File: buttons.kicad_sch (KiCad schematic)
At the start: 16 parts

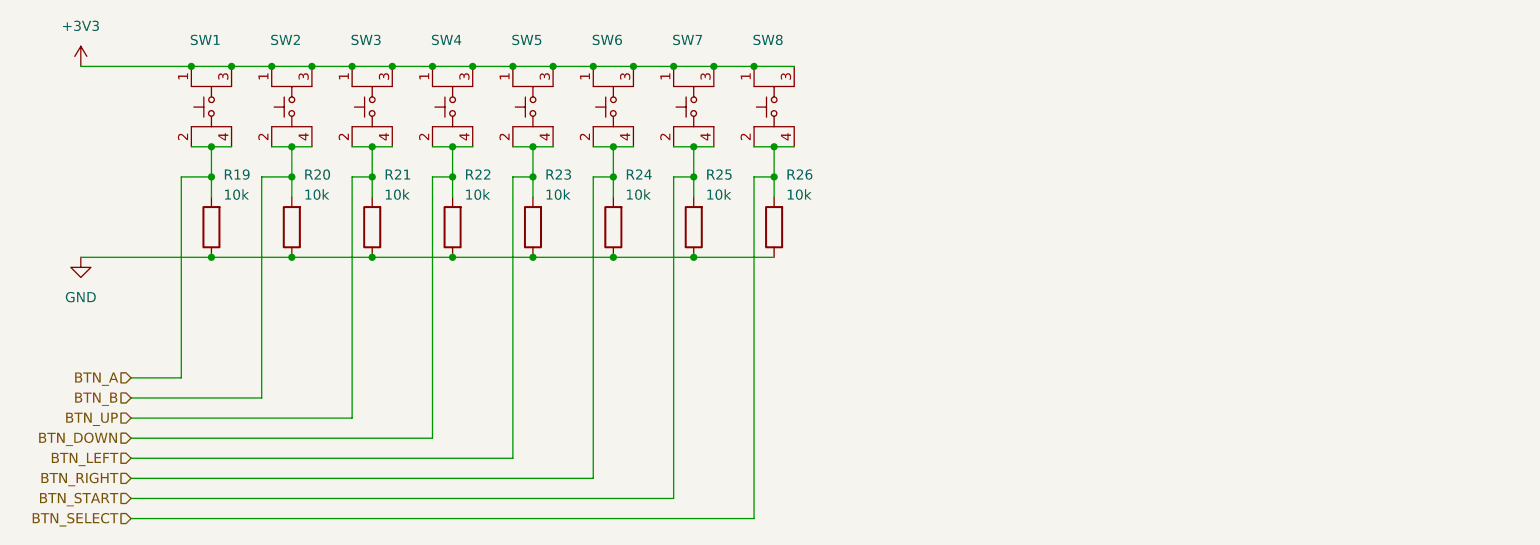
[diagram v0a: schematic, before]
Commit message: button debouncing and VDD decoupling
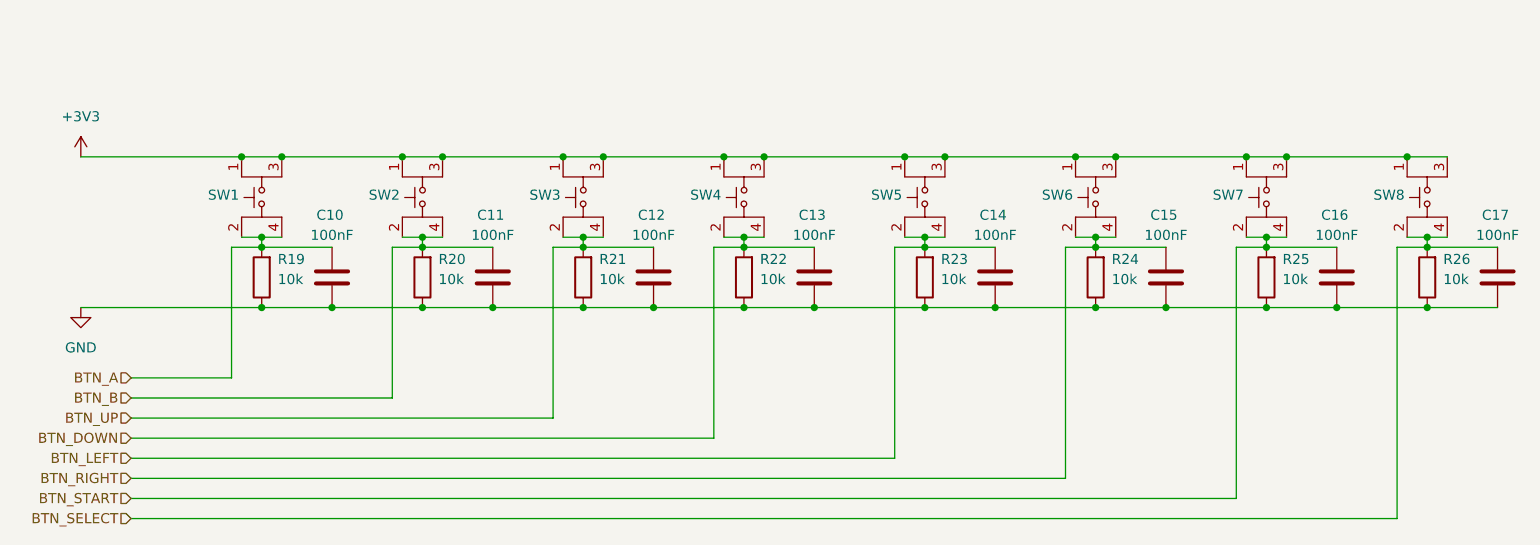
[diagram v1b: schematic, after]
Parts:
- added C10, C11, C12, C13, C14, C15, C16, C17: 100nF, Capacitor_SMD:C_0603_1608Metric, symbol Device:C
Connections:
- net BTN_A: now also C10.2
- net BTN_B: now also C11.2
- net BTN_DOWN: now also C13.2
- net BTN_LEFT: now also C14.2
- net BTN_RIGHT: now also C15.2
- net BTN_SELECT: now also C17.2
- net BTN_START: now also C16.2
- net BTN_UP: now also C12.2
- net GND: now also C10.1, C11.1, C12.1, C13.1, C14.1, C15.1, C16.1, C17.1
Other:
- moved on the sheet: R19, SW1

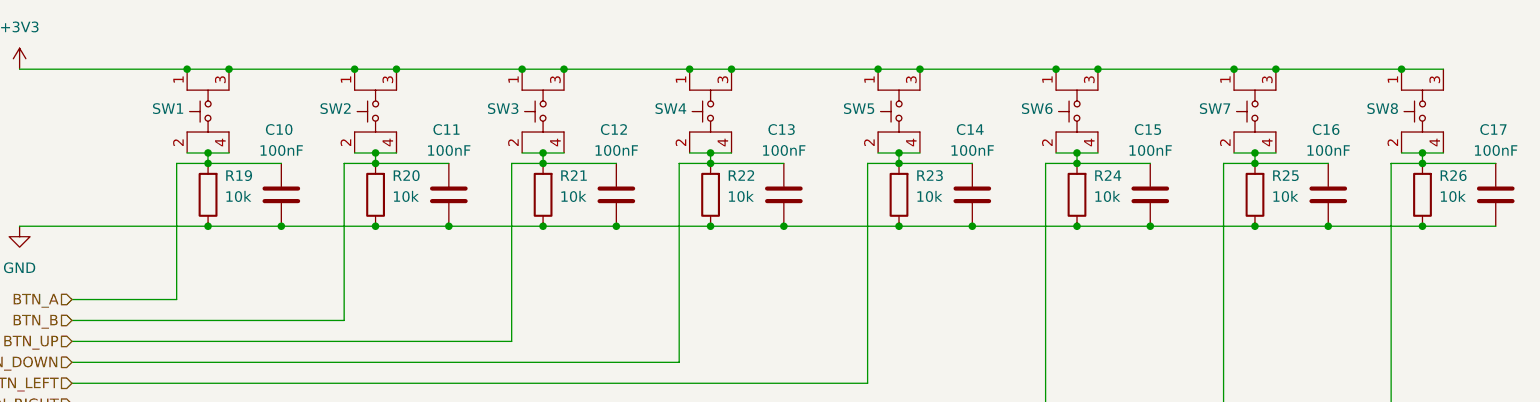
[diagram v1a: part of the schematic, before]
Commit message: schematic functional and includes current test setup
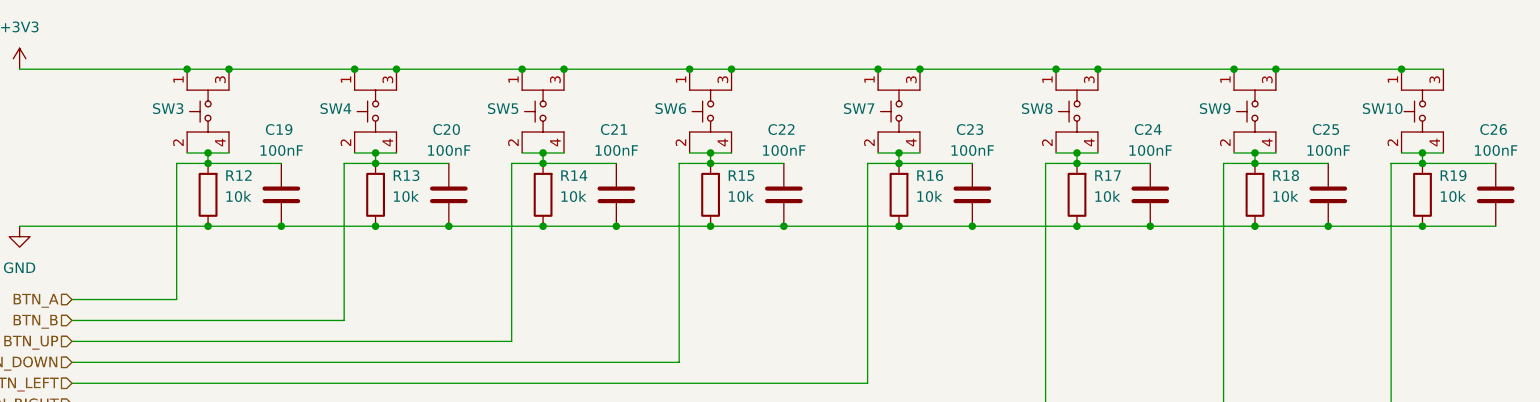
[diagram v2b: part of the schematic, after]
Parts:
- renumbered C10 to C19, C11 to C20, C12 to C21, C13 to C22, C14 to C23, C15 to C24, C16 to C25, C17 to C26, R19 to R12, R20 to R13, R21 to R14, R22 to R15, R23 to R16, R24 to R17, R25 to R18, R26 to R19, SW8 to SW10, SW1 to SW3, SW2 to SW4, SW3 to SW5, SW4 to SW6, SW5 to SW7, SW6 to SW8, SW7 to SW9
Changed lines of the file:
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@@
 		(on_board yes)
 		(dnp no)
-		(property "Reference" "SW7"
+		(property "Reference" "SW9"
 			(at 213.614 70.866 0)
 			(effects
@@
 			(project "gameboy"
 				(path "/f4643692-c319-40a7-82a2-3e775c0a417f/063c3b87-40d2-45e5-b5e2-db9e0e7c1214"
-					(reference "SW7")
+					(reference "SW9")
 					(unit 1)
 				)
@@
 		(on_board yes)
 		(dnp no)
-		(property "Reference" "R22"
+		(property "Reference" "R15"
 			(at 154.432 78.994 0)
 			(effects
@@
 			(project "gameboy"
 				(path "/f4643692-c319-40a7-82a2-3e775c0a417f/063c3b87-40d2-45e5-b5e2-db9e0e7c1214"
-					(reference "R22")
+					(reference "R15")
 					(unit 1)
 				)
@@
 		(on_board yes)
 		(dnp no)
-		(property "Reference" "C16"
+		(property "Reference" "C25"
 			(at 227.076 73.406 0)
 			(effects
@@
 			(project "gameboy"
 				(path "/f4643692-c319-40a7-82a2-3e775c0a417f/063c3b87-40d2-45e5-b5e2-db9e0e7c1214"
-					(reference "C16")
+					(reference "C25")
 					(unit 1)
 				)
@@
 		(on_board yes)
 		(dnp no)
-		(property "Reference" "SW1"
+		(property "Reference" "SW3"
 			(at 86.614 70.866 0)
 			(effects
@@
 			(project "gameboy"
 				(path "/f4643692-c319-40a7-82a2-3e775c0a417f/063c3b87-40d2-45e5-b5e2-db9e0e7c1214"
-					(reference "SW1")
+					(reference "SW3")
 					(unit 1)
 				)
@@
 		(on_board yes)
 		(dnp no)
-		(property "Reference" "R23"
+		(property "Reference" "R16"
 			(at 177.292 78.994 0)
 			(effects
@@
 			(project "gameboy"
 				(path "/f4643692-c319-40a7-82a2-3e775c0a417f/063c3b87-40d2-45e5-b5e2-db9e0e7c1214"
-					(reference "R23")
+					(reference "R16")
 					(unit 1)
 				)
@@
 		(on_board yes)
 		(dnp no)
-		(property "Reference" "SW4"
+		(property "Reference" "SW6"
 			(at 147.574 70.866 0)
 			(effects
@@
 			(project "gameboy"
 				(path "/f4643692-c319-40a7-82a2-3e775c0a417f/063c3b87-40d2-45e5-b5e2-db9e0e7c1214"
-					(reference "SW4")
+					(reference "SW6")
 					(unit 1)
 				)
@@
 		(on_board yes)
 		(dnp no)
-		(property "Reference" "R25"
+		(property "Reference" "R18"
 			(at 220.472 78.994 0)
 			(effects
@@
 			(project "gameboy"
 				(path "/f4643692-c319-40a7-82a2-3e775c0a417f/063c3b87-40d2-45e5-b5e2-db9e0e7c1214"
-					(reference "R25")
+					(reference "R18")
 					(unit 1)
 				)
@@
 		(on_board yes)
 		(dnp no)
-		(property "Reference" "SW3"
+		(property "Reference" "SW5"
 			(at 127.254 70.866 0)
 			(effects
@@
 			(project "gameboy"
 				(path "/f4643692-c319-40a7-82a2-3e775c0a417f/063c3b87-40d2-45e5-b5e2-db9e0e7c1214"
-					(reference "SW3")
+					(reference "SW5")
 					(unit 1)
 				)
@@
 		(on_board yes)
 		(dnp no)
-		(property "Reference" "C13"
+		(property "Reference" "C22"
 			(at 161.036 73.406 0)
 			(effects
@@
 			(project "gameboy"
 				(path "/f4643692-c319-40a7-82a2-3e775c0a417f/063c3b87-40d2-45e5-b5e2-db9e0e7c1214"
-					(reference "C13")
+					(reference "C22")
 					(unit 1)
 				)
@@
 		(on_board yes)
 		(dnp no)
-		(property "Reference" "C12"
+		(property "Reference" "C21"
 			(at 140.716 73.406 0)
 			(effects
@@
 			(project "gameboy"
 				(path "/f4643692-c319-40a7-82a2-3e775c0a417f/063c3b87-40d2-45e5-b5e2-db9e0e7c1214"
-					(reference "C12")
+					(reference "C21")
 					(unit 1)
 				)
@@
 		(on_board yes)
 		(dnp no)
-		(property "Reference" "C14"
+		(property "Reference" "C23"
 			(at 183.896 73.406 0)
 			(effects
@@
 			(project "gameboy"
 				(path "/f4643692-c319-40a7-82a2-3e775c0a417f/063c3b87-40d2-45e5-b5e2-db9e0e7c1214"
-					(reference "C14")
+					(reference "C23")
 					(unit 1)
 				)
@@
 		(on_board yes)
 		(dnp no)
-		(property "Reference" "SW2"
+		(property "Reference" "SW4"
 			(at 106.934 70.866 0)
 			(effects
@@
 			(project "gameboy"
 				(path "/f4643692-c319-40a7-82a2-3e775c0a417f/063c3b87-40d2-45e5-b5e2-db9e0e7c1214"
-					(reference "SW2")
+					(reference "SW4")
 					(unit 1)
 				)
@@
 		(on_board yes)
 		(dnp no)
-		(property "Reference" "C11"
+		(property "Reference" "C20"
 			(at 120.396 73.406 0)
 			(effects
@@
 			(project "gameboy"
 				(path "/f4643692-c319-40a7-82a2-3e775c0a417f/063c3b87-40d2-45e5-b5e2-db9e0e7c1214"
-					(reference "C11")
+					(reference "C20")
 					(unit 1)
 				)
@@
 		(on_board yes)
 		(dnp no)
-		(property "Reference" "C15"
+		(property "Reference" "C24"
 			(at 205.486 73.406 0)
 			(effects
@@
 			(project "gameboy"
 				(path "/f4643692-c319-40a7-82a2-3e775c0a417f/063c3b87-40d2-45e5-b5e2-db9e0e7c1214"
-					(reference "C15")
+					(reference "C24")
 					(unit 1)
 				)
@@
 		(on_board yes)
 		(dnp no)
-		(property "Reference" "SW6"
+		(property "Reference" "SW8"
 			(at 192.024 70.866 0)
 			(effects
@@
 			(project "gameboy"
 				(path "/f4643692-c319-40a7-82a2-3e775c0a417f/063c3b87-40d2-45e5-b5e2-db9e0e7c1214"
-					(reference "SW6")
+					(reference "SW8")
 					(unit 1)
 				)
@@
 		(on_board yes)
 		(dnp no)
-		(property "Reference" "R26"
+		(property "Reference" "R19"
 			(at 240.792 78.994 0)
 			(effects
@@
 			(project "gameboy"
 				(path "/f4643692-c319-40a7-82a2-3e775c0a417f/063c3b87-40d2-45e5-b5e2-db9e0e7c1214"
-					(reference "R26")
+					(reference "R19")
 					(unit 1)
 				)
@@
 		(on_board yes)
 		(dnp no)
-		(property "Reference" "R24"
+		(property "Reference" "R17"
 			(at 198.882 78.994 0)
 			(effects
@@
 			(project "gameboy"
 				(path "/f4643692-c319-40a7-82a2-3e775c0a417f/063c3b87-40d2-45e5-b5e2-db9e0e7c1214"
-					(reference "R24")
+					(reference "R17")
 					(unit 1)
 				)
@@
 		(on_board yes)
 		(dnp no)
-		(property "Reference" "R21"
+		(property "Reference" "R14"
 			(at 134.112 78.994 0)
 			(effects
@@
 			(project "gameboy"
 				(path "/f4643692-c319-40a7-82a2-3e775c0a417f/063c3b87-40d2-45e5-b5e2-db9e0e7c1214"
-					(reference "R21")
+					(reference "R14")
 					(unit 1)
 				)
@@
 		(on_board yes)
 		(dnp no)
-		(property "Reference" "SW5"
+		(property "Reference" "SW7"
 			(at 170.434 70.866 0)
 			(effects
@@
 			(project "gameboy"
 				(path "/f4643692-c319-40a7-82a2-3e775c0a417f/063c3b87-40d2-45e5-b5e2-db9e0e7c1214"
-					(reference "SW5")
+					(reference "SW7")
 					(unit 1)
 				)
@@
 		(dnp no)
 		(fields_autoplaced yes)
-		(property "Reference" "#PWR013"
+		(property "Reference" "#PWR021"
 			(at 68.58 69.85 0)
 			(effects
@@
 			(project "gameboy"
 				(path "/f4643692-c319-40a7-82a2-3e775c0a417f/063c3b87-40d2-45e5-b5e2-db9e0e7c1214"
-					(reference "#PWR013")
+					(reference "#PWR021")
 					(unit 1)
 				)
@@
 		(on_board yes)
 		(dnp no)
-		(property "Reference" "R20"
+		(property "Reference" "R13"
 			(at 113.792 78.994 0)
 			(effects
@@
 			(project "gameboy"
 				(path "/f4643692-c319-40a7-82a2-3e775c0a417f/063c3b87-40d2-45e5-b5e2-db9e0e7c1214"
-					(reference "R20")
+					(reference "R13")
 					(unit 1)
 				)
@@
 		(on_board yes)
 		(dnp no)
-		(property "Reference" "C17"
+		(property "Reference" "C26"
 			(at 247.396 73.406 0)
 			(effects
@@
 			(project "gameboy"
 				(path "/f4643692-c319-40a7-82a2-3e775c0a417f/063c3b87-40d2-45e5-b5e2-db9e0e7c1214"
-					(reference "C17")
+					(reference "C26")
 					(unit 1)
 				)
@@
 		(on_board yes)
 		(dnp no)
-		(property "Reference" "C10"
+		(property "Reference" "C19"
 			(at 100.076 73.406 0)
 			(effects
@@
 			(project "gameboy"
 				(path "/f4643692-c319-40a7-82a2-3e775c0a417f/063c3b87-40d2-45e5-b5e2-db9e0e7c1214"
-					(reference "C10")
+					(reference "C19")
 					(unit 1)
 				)
@@
 		(dnp no)
 		(fields_autoplaced yes)
-		(property "Reference" "#PWR014"
+		(property "Reference" "#PWR022"
 			(at 68.58 91.44 0)
 			(effects
@@
 			(project "gameboy"
 				(path "/f4643692-c319-40a7-82a2-3e775c0a417f/063c3b87-40d2-45e5-b5e2-db9e0e7c1214"
-					(reference "#PWR014")
+					(reference "#PWR022")
 					(unit 1)
 				)
@@
 		(on_board yes)
 		(dnp no)
-		(property "Reference" "SW8"
+		(property "Reference" "SW10"
 			(at 233.934 70.866 0)
 			(effects
@@
 			(project "gameboy"
 				(path "/f4643692-c319-40a7-82a2-3e775c0a417f/063c3b87-40d2-45e5-b5e2-db9e0e7c1214"
-					(reference "SW8")
+					(reference "SW10")
 					(unit 1)
 				)
@@
 		(on_board yes)
 		(dnp no)
-		(property "Reference" "R19"
+		(property "Reference" "R12"
 			(at 93.472 78.994 0)
 			(effects
@@
 			(project "gameboy"
 				(path "/f4643692-c319-40a7-82a2-3e775c0a417f/063c3b87-40d2-45e5-b5e2-db9e0e7c1214"
-					(reference "R19")
-					(unit 1)
-				)
+					(reference "R12")
+					(unit 1)
+				)

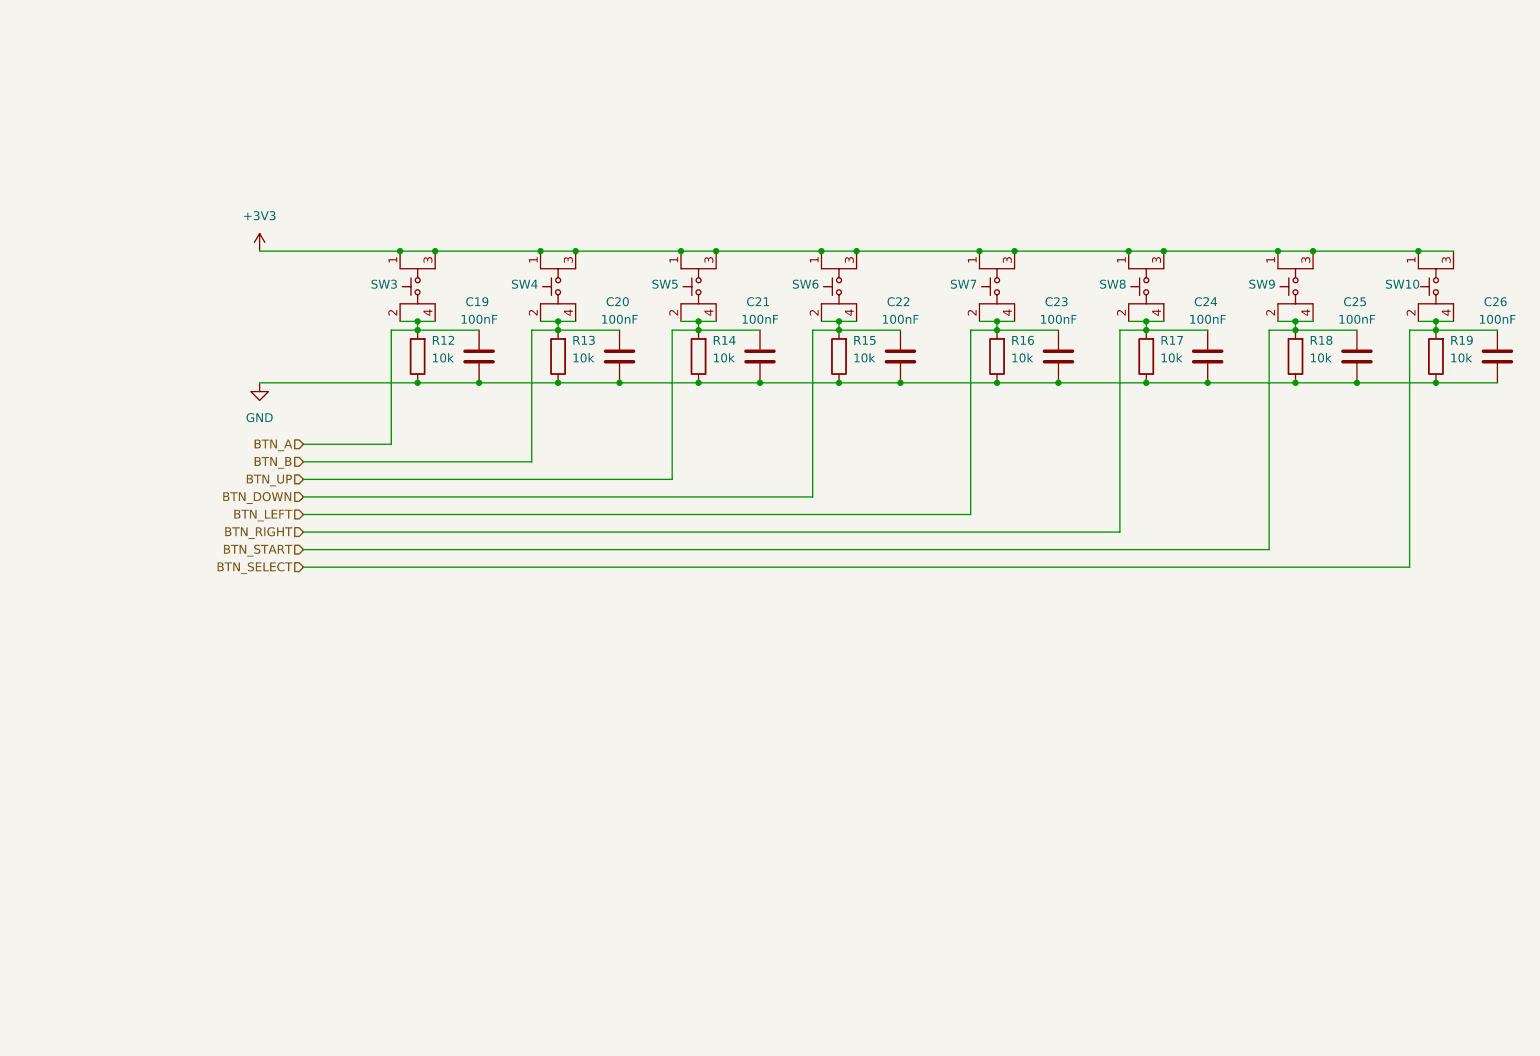
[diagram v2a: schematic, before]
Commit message: add amplifier mode selector, add drawing lcd
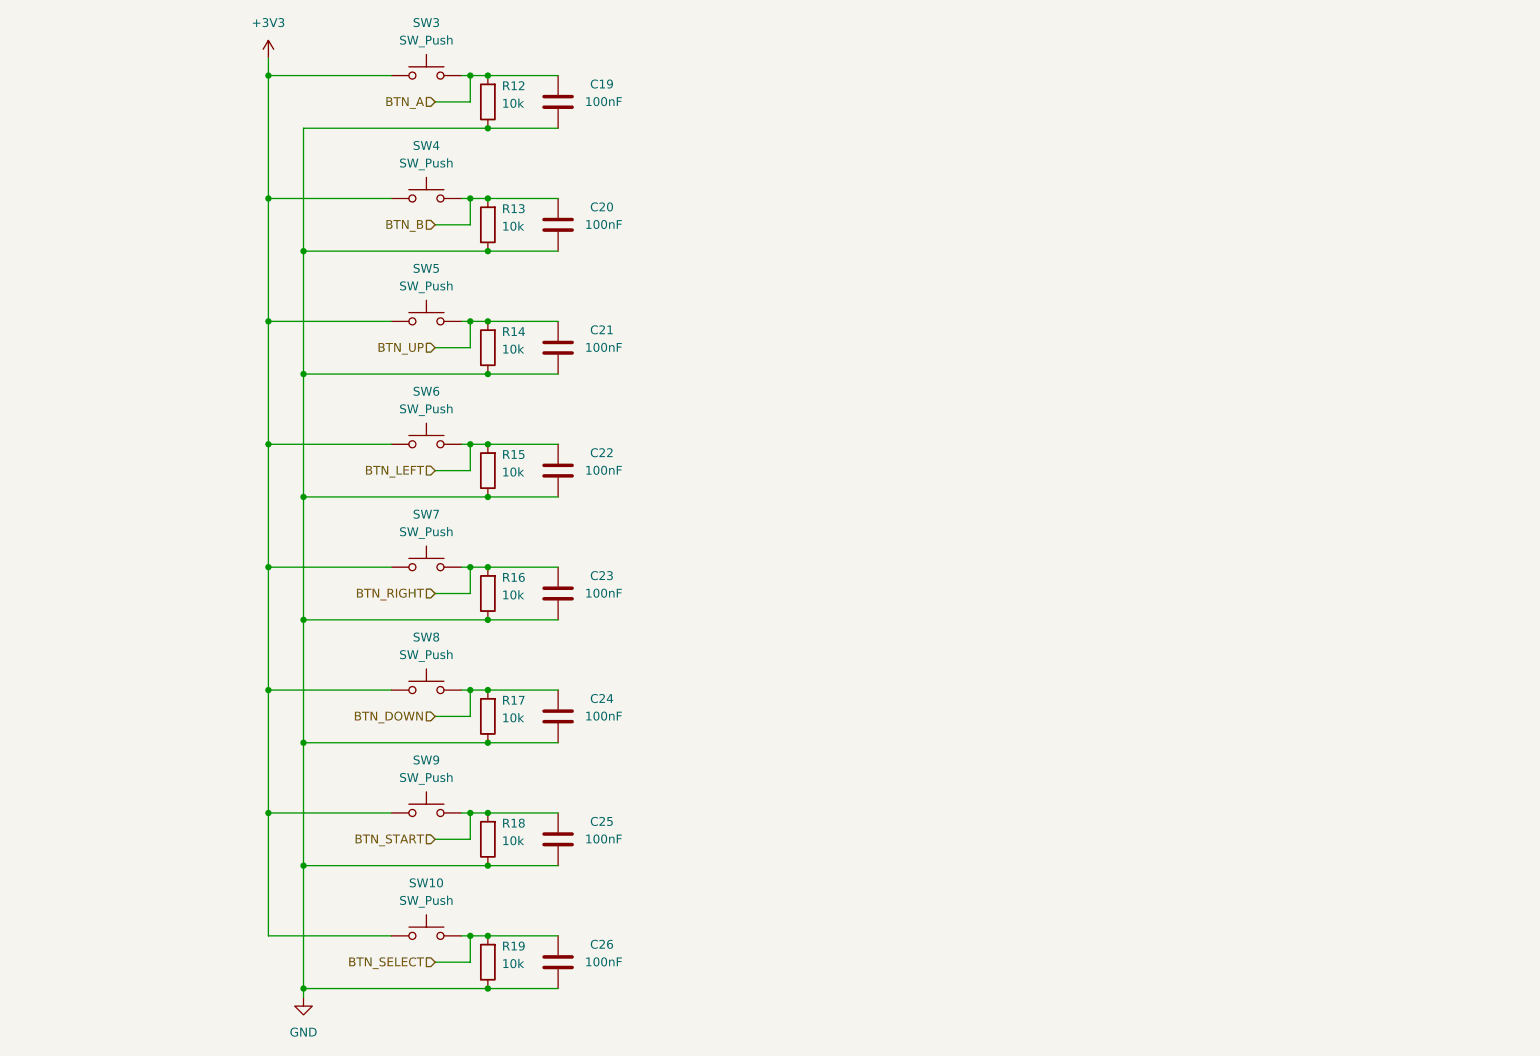
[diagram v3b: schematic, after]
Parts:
- removed SW10, SW3, SW4, SW5, SW6, SW7, SW8, SW9: ~, SKRRAAE010:SKRRAAE010, symbol SKRRAAE010:SKRRAAE010
- added SW10, SW3, SW4, SW5, SW6, SW7, SW8, SW9: SW_Push, Button_Switch_SMD:SW_Push_1TS009xxxx-xxxx-xxxx_6x6x5mm, symbol Switch:SW_Push
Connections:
- net +3V3: now also SW10.1, SW3.1, SW4.1, SW5.1, SW6.1, SW7.1, SW8.1, SW9.1
- net BTN_A: now also SW3.2
- net BTN_B: now also SW4.2
- net BTN_DOWN: now also C24.2, R17.2, SW8.2; no longer C22.2, R15.2
- net BTN_LEFT: now also C22.2, R15.2, SW6.2; no longer C23.2, R16.2
- net BTN_RIGHT: now also C23.2, R16.2, SW7.2; no longer C24.2, R17.2
- net BTN_SELECT: now also SW10.2
- net BTN_START: now also SW9.2
- net BTN_UP: now also SW5.2
